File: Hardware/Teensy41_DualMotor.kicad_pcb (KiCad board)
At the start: 2 copper layers, 116.8 x 66 mm, 43 parts, among them J1 Conn_02x18_Odd_Even, J10 Conn_02x05_Odd_Even, J2 Conn_01x05, J3 Conn_01x05, J4 Conn_01x05, J5 Conn_02x18_Odd_Even, J6 Conn_01x05, J7 Conn_01x05, J8 Conn_01x05, J9 Conn_02x05_Odd_Even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

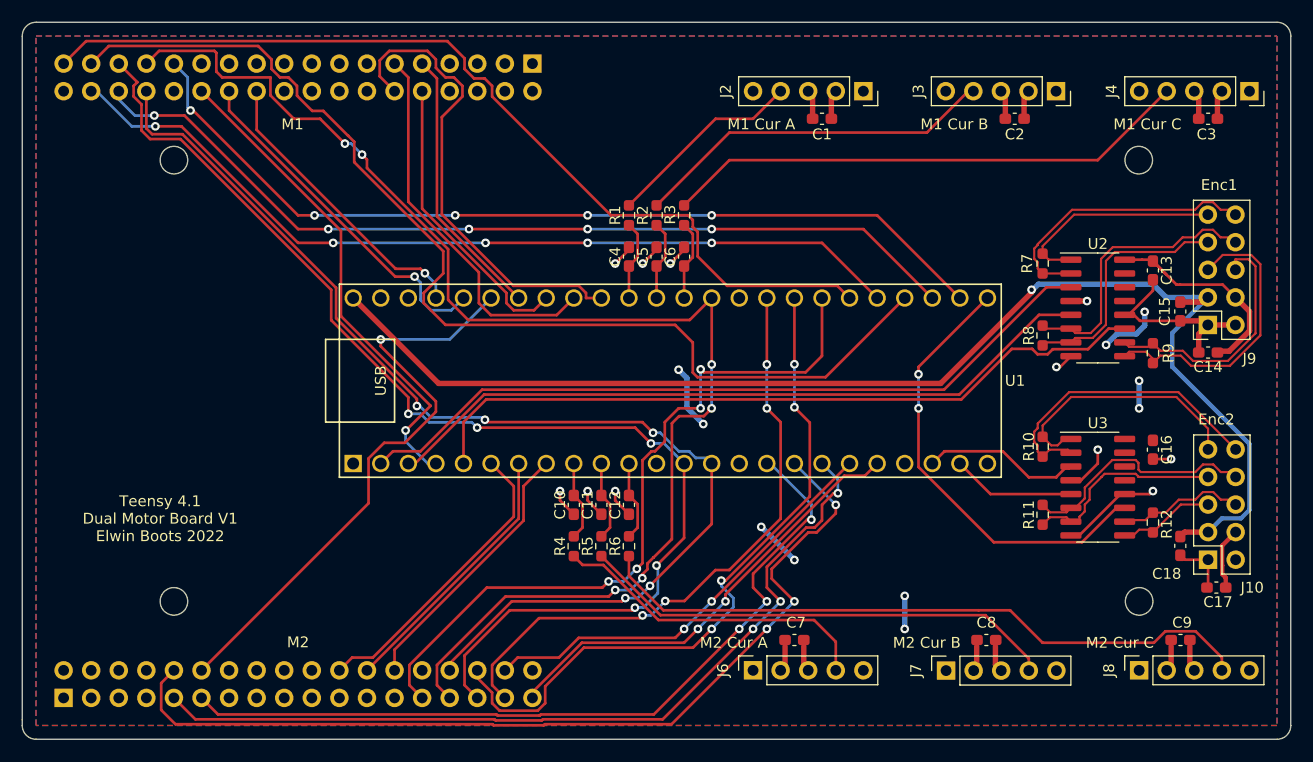
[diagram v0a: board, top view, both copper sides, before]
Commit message: added filters and solder bridges to select low side current sense or external inline current sense
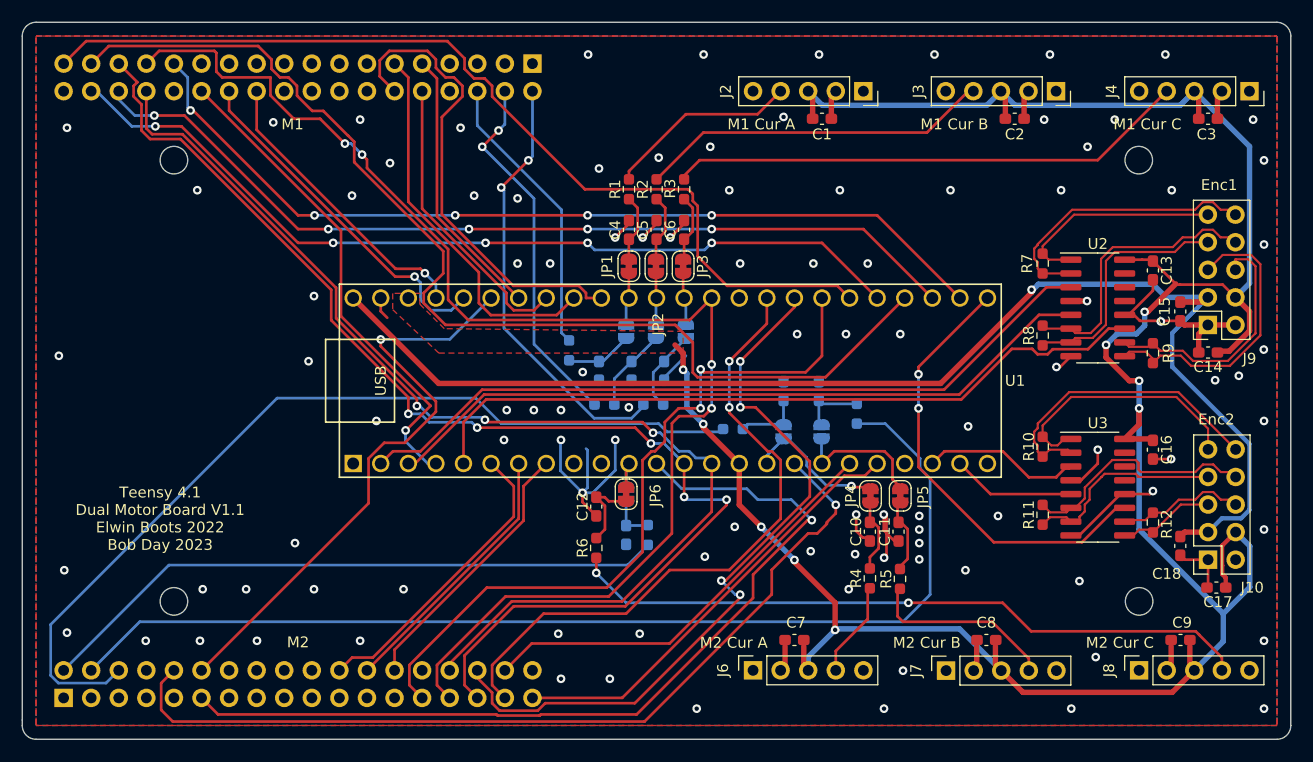
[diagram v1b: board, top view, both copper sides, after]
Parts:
- added C19: 15n, Capacitor_SMD:C_0603_1608Metric_Pad1.08x0.95mm_HandSolder, B.Cu at (77.2, 113.4)
- added C20: 15n, Capacitor_SMD:C_0603_1608Metric_Pad1.08x0.95mm_HandSolder, B.Cu at (80.2, 113.4)
- added C21: 15n, Capacitor_SMD:C_0603_1608Metric_Pad1.08x0.95mm_HandSolder, B.Cu at (83.2, 113.4)
- added C22: 15n, Capacitor_SMD:C_0603_1608Metric_Pad1.08x0.95mm_HandSolder, B.Cu at (94.2, 115.2)
- added C23: 15n, Capacitor_SMD:C_0603_1608Metric_Pad1.08x0.95mm_HandSolder, B.Cu at (97.5, 115.2)
- added C24: 15n, Capacitor_SMD:C_0603_1608Metric_Pad1.08x0.95mm_HandSolder, B.Cu at (79.8, 128.5)
- added JP1: PH_A_SEL, Jumper:SolderJumper-2_P1.3mm_Bridged_RoundedPad1.0x1.5mm, F.Cu at (80.0, 103.8)
- added JP10: LS_A2_SEL, Jumper:SolderJumper-2_P1.3mm_Open_RoundedPad1.0x1.5mm, B.Cu at (94.2, 119.0)
- added JP11: LS_B2_SEL, Jumper:SolderJumper-2_P1.3mm_Open_RoundedPad1.0x1.5mm, B.Cu at (97.8, 119.0)
- added JP12: LS_C2_SEL, Jumper:SolderJumper-2_P1.3mm_Open_RoundedPad1.0x1.5mm, B.Cu at (79.8, 124.8)
- added JP2: PH_B_SEL, Jumper:SolderJumper-2_P1.3mm_Bridged_RoundedPad1.0x1.5mm, F.Cu at (82.5, 103.8)
- added JP3: PH_C_SEL, Jumper:SolderJumper-2_P1.3mm_Bridged_RoundedPad1.0x1.5mm, F.Cu at (85.0, 103.8)
- added JP4: PH_A2_SEL, Jumper:SolderJumper-2_P1.3mm_Bridged_RoundedPad1.0x1.5mm, F.Cu at (102.2, 124.9)
- added JP5: PH_B2_SEL, Jumper:SolderJumper-2_P1.3mm_Bridged_RoundedPad1.0x1.5mm, F.Cu at (105.0, 124.9)
- added JP6: PH_C2_SEL, Jumper:SolderJumper-2_P1.3mm_Bridged_RoundedPad1.0x1.5mm, F.Cu at (79.8, 124.8)
- added JP7: LS_A_SEL, Jumper:SolderJumper-2_P1.3mm_Open_RoundedPad1.0x1.5mm, B.Cu at (79.8, 109.8)
- added JP8: LS_B_SEL, Jumper:SolderJumper-2_P1.3mm_Open_RoundedPad1.0x1.5mm, B.Cu at (82.5, 109.8)
- added JP9: LS_C_SEL, Jumper:SolderJumper-2_P1.3mm_Open_RoundedPad1.0x1.5mm, B.Cu at (85.2, 109.8)
- added R13: 1k, Resistor_SMD:R_0603_1608Metric_Pad0.98x0.95mm_HandSolder, B.Cu at (74.5, 111.5)
- added R14: 1k, Resistor_SMD:R_0603_1608Metric_Pad0.98x0.95mm_HandSolder, B.Cu at (77.8, 116.5)
- added R15: 1k, Resistor_SMD:R_0603_1608Metric_Pad0.98x0.95mm_HandSolder, B.Cu at (82.2, 116.5)
- added R16: 1k, Resistor_SMD:R_0603_1608Metric_Pad0.98x0.95mm_HandSolder, B.Cu at (89.6, 118.8)
- added R17: 1k, Resistor_SMD:R_0603_1608Metric_Pad0.98x0.95mm_HandSolder, B.Cu at (101.0, 117.3)
- added R18: 1k, Resistor_SMD:R_0603_1608Metric_Pad0.98x0.95mm_HandSolder, B.Cu at (81.8, 128.5)
- moved R5 27.7 mm to (105.0, 132.6)
- moved C11 27.5 mm to (104.8, 128.2)
- moved R4 27.4 mm to (102.2, 132.5)
- moved C10 27.4 mm to (102.2, 128.2)
- moved C12 3.01 mm to (77.0, 125.9)
- moved R6 3.01 mm to (77.0, 129.7)
- moved C4 2.47 mm to (80.0, 100.4)
- moved C5 2.47 mm to (82.5, 100.4)
- moved C6 2.47 mm to (85.1, 100.4)
- moved R1 2.40 mm to (80.0, 96.7)
- moved R2 2.40 mm to (82.5, 96.7)
- moved R3 2.40 mm to (85.1, 96.7)
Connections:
- C10 pad 1: I_PH_A2_Filt -> Net-(JP4-A)
- C11 pad 1: I_PH_B2_Filt -> Net-(JP5-A)
- C12 pad 1: I_PH_C2_Filt -> Net-(JP6-A)
- C4 pad 1: I_PH_A_Filt -> Net-(JP1-A)
- C5 pad 1: I_PH_B_Filt -> Net-(JP2-A)
- C6 pad 1: I_PH_C_Filt -> Net-(JP3-A)
- J1 pad 2: unconnected-(J1-Pad2) -> I_LS_C
- J1 pad 4: unconnected-(J1-Pad4) -> I_LS_B
- J1 pad 6: unconnected-(J1-Pad6) -> I_LS_A
- J5 pad 2: unconnected-(J5-Pad2) -> I_LS_C2
- J5 pad 4: unconnected-(J5-Pad4) -> I_LS_B2
- J5 pad 6: unconnected-(J5-Pad6) -> I_LS_A2
- R1 pad 2: I_PH_A_Filt -> Net-(JP1-A)
- R2 pad 2: I_PH_B_Filt -> Net-(JP2-A)
- R3 pad 2: I_PH_C_Filt -> Net-(JP3-A)
- R4 pad 2: I_PH_A2_Filt -> Net-(JP4-A)
- R5 pad 2: I_PH_B2_Filt -> Net-(JP5-A)
- R6 pad 2: I_PH_C2_Filt -> Net-(JP6-A)
- U1 pad 10: I_PH_B2_Filt -> unconnected-(U1-8_TX2_IN1-Pad10)
- U1 pad 12: unconnected-(U1-Pad12) -> EMF-A2
- U1 pad 16: EMF-A2 -> I_PH_A2_Filt
- U1 pad 18: EMF-C2 -> I_PH_B2_Filt
- U1 pad 9: I_PH_A2_Filt -> unconnected-(U1-7_RX2_OUT1A-Pad9)
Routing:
- net +3V3: track 63.4 -> 233.7 mm, vias 10 -> 9
- net I_LS_B2: track 0.00 -> 100.2 mm
- net I_LS_A2: track 0.00 -> 83.7 mm
- net EMF-C2: track 78.5 -> 0.00 mm, vias 3 -> 0
- net I_LS_C2: track 0.00 -> 58.6 mm
- net I_LS_C: track 0.00 -> 40.0 mm, vias 0 -> 2
- net I_LS_B: track 0.00 -> 34.0 mm, vias 0 -> 2
- net GND: track 71.0 -> 98.0 mm, vias 11 -> 103
- net I_PH_B2: track 44.4 -> 17.4 mm
- net I_LS_A: track 0.00 -> 26.5 mm
- net I_PH_A2: track 30.0 -> 8.89 mm
- net EMF-A2: track 74.7 -> 82.7 mm, vias 3 -> 1
- net Net-(JP6-A): track 0.00 -> 7.86 mm
- net Net-(JP8-A): track 0.00 -> 7.76 mm
- net Net-(JP9-A): track 0.00 -> 7.72 mm
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- added copper zone on F.Cu, net GND
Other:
- board text added: "Teensy 4.1 Dual Motor Board V1.1 Elwin Boots 2022 Bob Day 2023"
- board text removed: "Teensy 4.1 Dual Motor Board V1 Elwin Boots 2022"
